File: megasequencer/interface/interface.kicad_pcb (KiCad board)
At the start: 2 copper layers, 99.1 x 99.1 mm, 55 parts, among them J1 INT_CLOCK_OUT, J10 OFFSET_A, J11 OFFSET_B, J12 OFFSET_C, J13 OFFSET_D, J14 OUTPUT_A, J15 OUTPUT_B, J16 OUTPUT_C, J17 OUTPUT_D, J18 OUTPUT_E, J19 OUTPUT_F, J2 EXT_CLOCK_IN, J20 TOP, J21 BOTTOM, J3 DIR_IN, J4 RESET_IN, J5 ZERO_IN, J6 STEP_OUT, J7 EXT_RATE_CV, J8 EXT_POS_CV, J9 PULSELEN_CV, SW1 CLOCK_SW, SW2 RESET_SW, SW3 ZERO_SW, SW4 SW_SPDT

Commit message: Finish interface and continue with brain
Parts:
- J20, J21: moved to B.Cu
- SW4: value SW_SPDT -> SEQ_DIR
- moved J21 153.8 mm to (73.7, 121.9), turned to 90 degrees
- moved R9 25.4 mm to (87.6, 110.5), turned to 90 degrees
- moved R12 21.6 mm to (87.6, 92.7)
- moved RV3 21.6 mm to (99.1, 114.3)
- moved RV6 21.6 mm to (99.1, 92.7)
- moved SW4 18.8 mm to (30.5, 104.8), turned to 0 degrees
- moved SW2 7.73 mm to (61.0, 109.2), turned to 180 degrees
- moved R11 7.18 mm to (106.7, 92.7), turned to 90 degrees
- moved R7 3.81 mm to (68.6, 110.5), turned to 90 degrees
- moved R8 3.81 mm to (106.7, 110.5), turned to 90 degrees
- moved SW3 3.24 mm to (42.5, 104.8)
- turned J20 to 90 degrees
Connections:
- H1 pad 1: Net-(H1-Pad1) -> GND
- H2 pad 1: Net-(H2-Pad1) -> GND
- H3 pad 1: Net-(H3-Pad1) -> GND
- H4 pad 1: Net-(H4-Pad1) -> GND
- J20 pad 1: Net-(J20-Pad1) -> GND
- J21 pad 1: Net-(J21-Pad1) -> GND
- J21 pad 10: Net-(J21-Pad10) -> /PULSELEN_A
- J21 pad 11: Net-(J21-Pad11) -> /EXT_RATE_A
- J21 pad 12: Net-(J21-Pad12) -> /SEQ_RESET_D
- J21 pad 13: Net-(J21-Pad13) -> /SEQ_ZERO_D
- J21 pad 14: Net-(J21-Pad14) -> /SEQ_DIR_D
- J21 pad 15: Net-(J21-Pad15) -> +5V
- J21 pad 16: Net-(J21-Pad16) -> GND
- J21 pad 9: Net-(J21-Pad9) -> /EXT_POS_A
- RV1 pad 1: GND -> +5V
- RV1 pad 3: +5V -> GND
- RV2 pad 1: GND -> +5V
- RV2 pad 3: +5V -> GND
- RV3 pad 1: GND -> +5V
- RV3 pad 3: +5V -> GND
- RV4 pad 1: GND -> Net-(J7-PadT)
- RV4 pad 3: Net-(J7-PadT) -> GND
- RV5 pad 1: GND -> Net-(J8-PadT)
- RV5 pad 3: Net-(J8-PadT) -> GND
- RV6 pad 1: GND -> Net-(J9-PadT)
- RV6 pad 3: Net-(J9-PadT) -> GND
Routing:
- net +5V: track 6.50 -> 164.4 mm
- net /EXT_POS_A: track 0.00 -> 72.1 mm
- net /PULSELEN_A: track 0.00 -> 54.9 mm
- net /SEQ_RESET_D: track 0.00 -> 43.2 mm
- net Net-(J8-PadT): track 0.00 -> 42.1 mm
- net /EXT_RATE_A: track 0.00 -> 39.1 mm
- net Net-(J3-PadTN): track 0.00 -> 35.5 mm
- net /SEQ_ZERO_D: track 0.00 -> 32.9 mm
- net /SEQ_DIR_D: track 0.00 -> 29.6 mm
- net Net-(J9-PadT): track 0.00 -> 28.6 mm
- net Net-(J7-PadT): track 0.00 -> 26.3 mm
- net Net-(R12-Pad2): track 0.00 -> 12.1 mm
- net Net-(R10-Pad2): track 0.00 -> 12.1 mm
- net Net-(R11-Pad2): track 0.00 -> 12.1 mm
- net Net-(D8-Pad2): track 0.00 -> 11.8 mm
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- added copper zone on B.Cu, net GND
- added copper zone on F.Cu, net GND
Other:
- board text added: "+5V"
- board text added: "A"
- board text added: "A+"
- board text added: "B"
- board text added: "B+"
- board text added: "C"
- board text added: "C+"
- board text added: "D"
- board text added: "D+"
- board text added: "DIR"
- board text added: "Direction"
- board text added: "E"
- board text added: "ExtClk"
- board text added: "ExtPosition"
- board text added: "ExtRate"
- board text added: "F"
- board text added: "GND"
- board text added: "IntClk"
- board text added: "MegaSequencer Interface Johan Egneblad 2019-12-26"
- board text added: "NC"
- board text added: "Pulse"
- board text added: "PulseLength"
- board text added: "Reset"
- board text added: "Zero"

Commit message: Almost done now with both pcbs
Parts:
- added J22: RIGHT, Connector_PinHeader_2.54mm:PinHeader_1x04_P2.54mm_Vertical, B.Cu at (121.9, 66.0)
- J21: footprint Connector_PinHeader_2.54mm:PinHeader_1x16_P2.54mm_Vertical -> Connector_PinHeader_2.54mm:PinHeader_1x08_P2.54mm_Vertical
- moved J21 20.3 mm to (53.3, 121.9)
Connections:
- J21 pad 4: Net-(J21-Pad4) -> /SEQ_RESET_D
- J21 pad 5: Net-(J21-Pad5) -> /SEQ_ZERO_D
- J21 pad 6: Net-(J21-Pad6) -> /SEQ_DIR_D
- J21 pad 7: Net-(J21-Pad7) -> +5V
- J21 pad 8: Net-(J21-Pad8) -> GND
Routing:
- net /EXT_RATE_A: track 39.1 -> 74.4 mm
- net /EXT_POS_A: track 72.1 -> 53.5 mm
- net /PULSELEN_A: track 54.9 -> 55.4 mm
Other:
- board text added: "MegaSequencer Interface Johan Egneblad 2019-12-28"
- board text added: "RIGHT:"
- board text removed: "MegaSequencer Interface Johan Egneblad 2019-12-26"

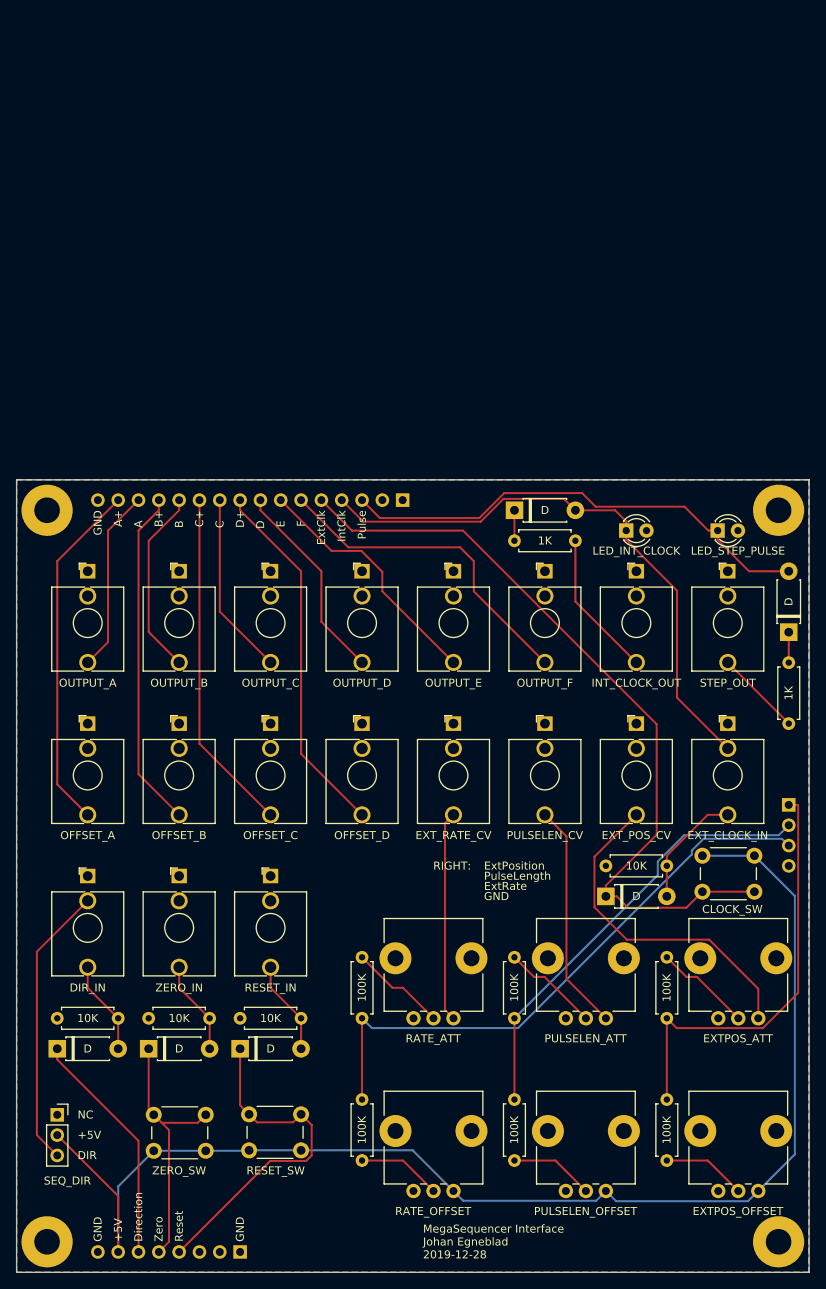
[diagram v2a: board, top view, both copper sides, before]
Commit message: Finish up labeling and fixa connector that was in the wrong direction
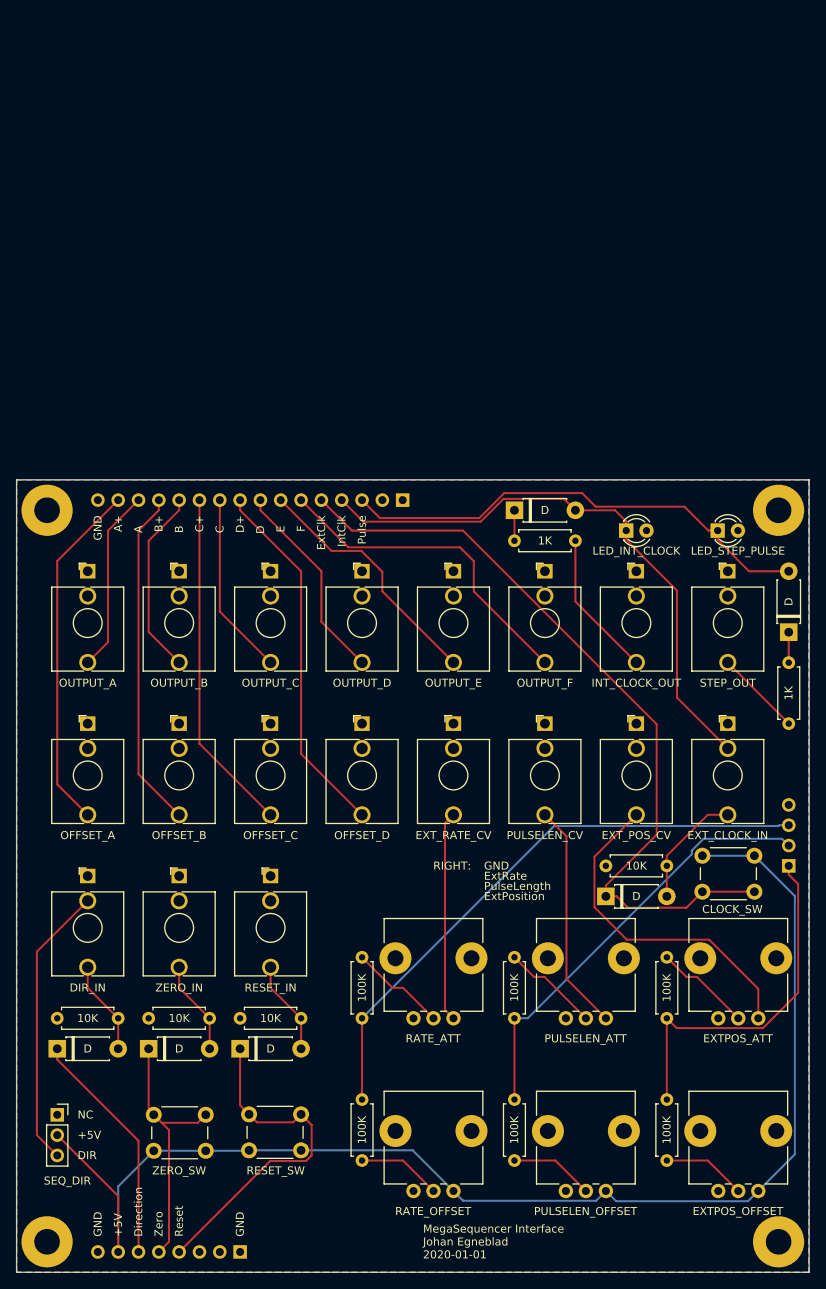
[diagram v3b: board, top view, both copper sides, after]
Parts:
- moved J22 7.62 mm to (121.9, 73.7), turned to 0 degrees
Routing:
- net /EXT_POS_A: track 53.5 -> 45.3 mm
- net /PULSELEN_A: track 55.4 -> 54.4 mm
- net /EXT_RATE_A: track 74.4 -> 73.5 mm
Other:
- board text added: "MegaSequencer Interface Johan Egneblad 2020-01-01"
- board text removed: "MegaSequencer Interface Johan Egneblad 2019-12-28"
